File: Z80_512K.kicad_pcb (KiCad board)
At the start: 2 copper layers, 73 x 55.5 mm, 24 parts, among them J1 USB_B_Mini, J2 EXPANSION-BUS, SW1 ON|OFF, SW2 Z80-RESET, U1 Z84C00/PLCC, U2 74HCT574, U3 SRAM-SOP32, U4 74HC138, U5 SST39SF040, U6 74HC74, U7 74HC00, Y1 CXO_DIP14

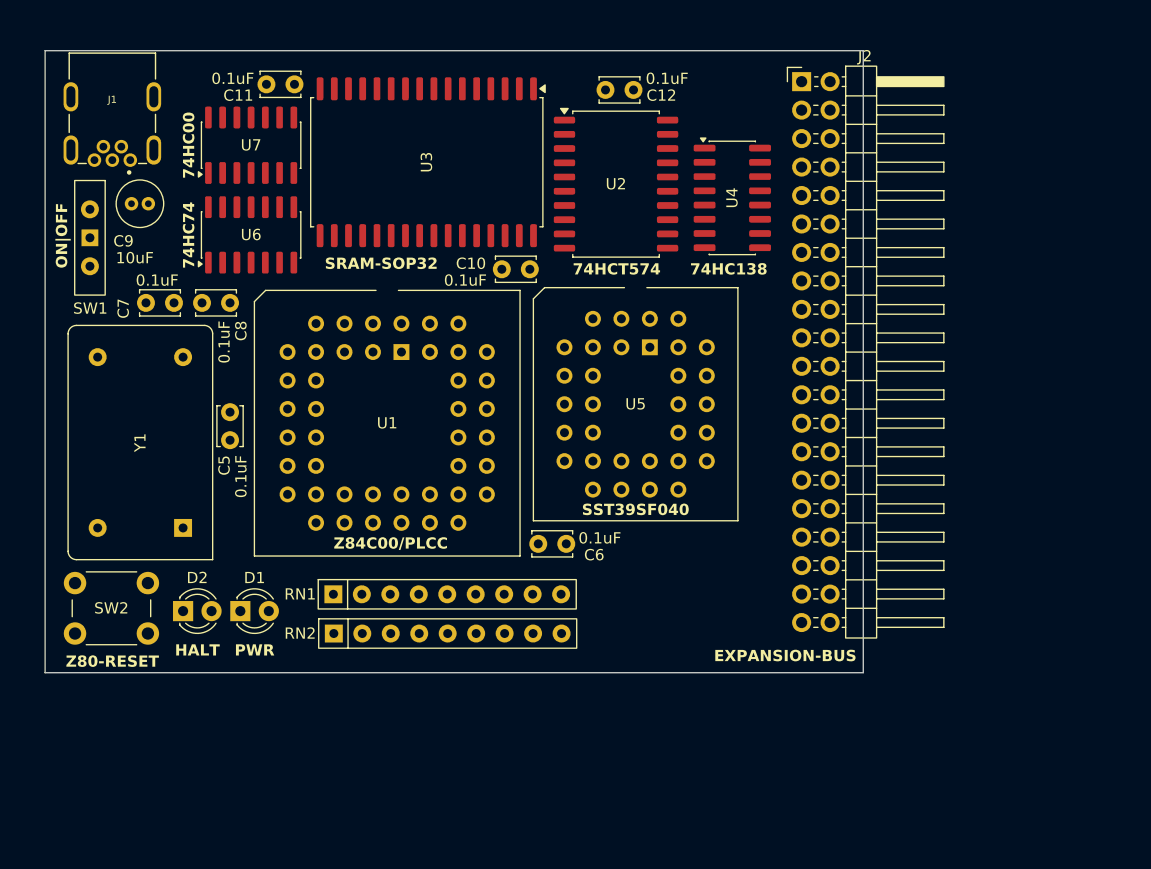
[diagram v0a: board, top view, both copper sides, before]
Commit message: Finished Routing Layout.
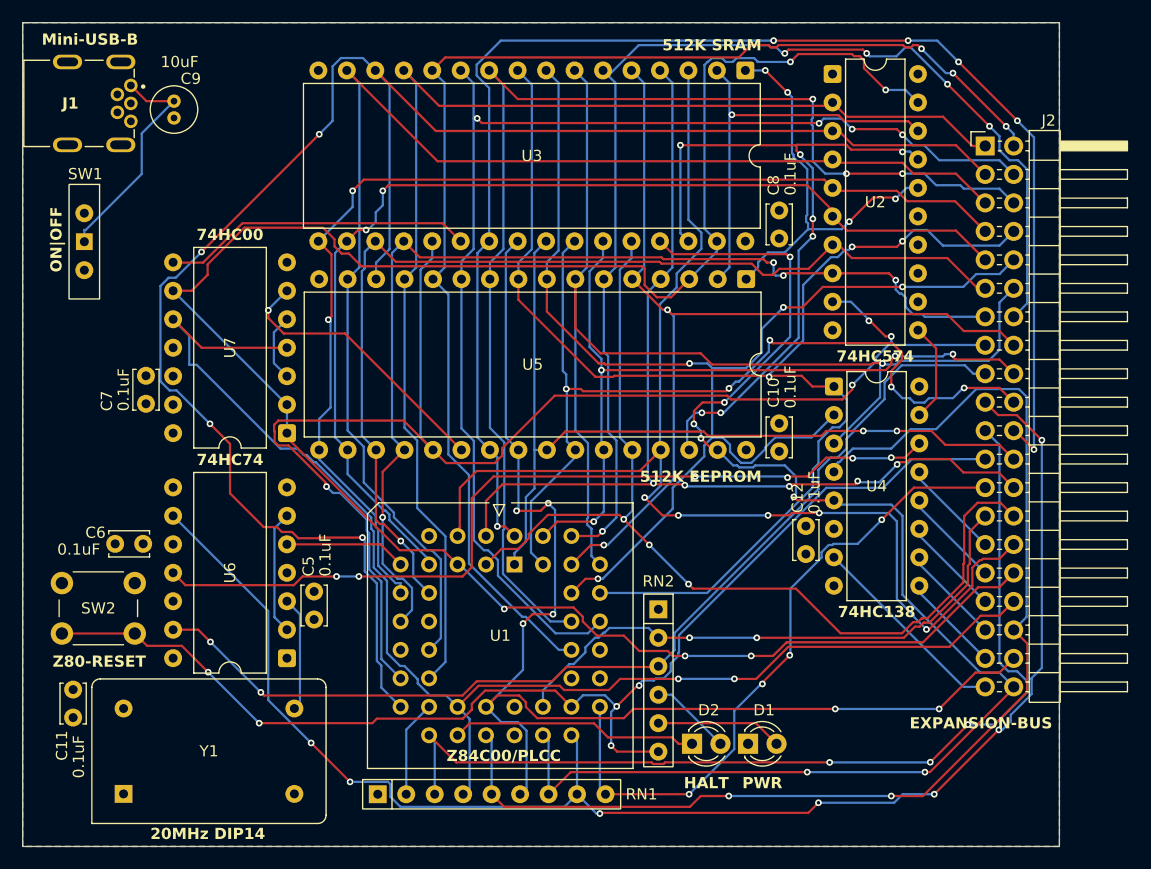
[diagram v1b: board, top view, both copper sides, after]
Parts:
- J1: value USB_B_Mini -> Mini-USB-B
- RN1: value RN_10K -> RN10K
- RN2: value RN_10K -> RN10K; footprint Resistor_THT:R_Array_SIP9 -> Resistor_THT:R_Array_SIP6
- U2: value 74HCT574 -> 74HC574; footprint Package_SO:SOP-20_7.5x12.8mm_P1.27mm -> Package_DIP:DIP-20_W7.62mm
- U3: value SRAM-SOP32 -> 512K SRAM; footprint Package_SO:SOP-32_11.305x20.495mm_P1.27mm -> Package_DIP:DIP-32_W15.24mm
- U4: footprint Package_SO:SOIC-16_3.9x9.9mm_P1.27mm -> Package_DIP:DIP-16_W7.62mm
- U5: value SST39SF040 -> 512K EEPROM; footprint Package_LCC:PLCC-32_THT-Socket -> Package_DIP:DIP-32_W15.24mm
- U6, U7: footprint Package_SO:SOIC-14_3.9x8.7mm_P1.27mm -> Package_DIP:DIP-14_W10.16mm
- Y1: value CXO_DIP14 -> 20MHz DIP14
- moved C11 59.9 mm to (107.0, 93.0), turned to 90 degrees
- moved C8 49.7 mm to (170.0, 47.8), turned to -90 degrees
- moved D2 46.9 mm to (162.2, 95.3)
- moved D1 46.8 mm to (167.2, 95.3)
- moved C12 44.2 mm to (172.4, 78.4), turned to 90 degrees
- moved C6 40.2 mm to (110.8, 77.5), turned to 0 degrees
- moved U6 37.9 mm to (126.1, 87.7), turned to 180 degrees
- moved U3 29.6 mm to (167.0, 35.3)
- moved RN2 29.0 mm to (159.2, 83.3), turned to -90 degrees
- moved C10 26.2 mm to (170.0, 66.8), turned to -90 degrees
- moved U7 25.9 mm to (126.1, 67.6), turned to 180 degrees
- moved Y1 24.3 mm to (111.5, 99.8), turned to 0 degrees
- moved U2 21.7 mm to (174.8, 35.6)
- moved U1 21.5 mm to (146.4, 79.3)
- moved U4 19.1 mm to (174.9, 63.5)
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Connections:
- RN1 pad 2: /MREQ -> /NMI
- RN1 pad 3: /IORQ -> /INT
- RN1 pad 4: /RD -> /MREQ
- RN1 pad 5: /WR -> /IORQ
- RN1 pad 6: /WAIT -> /RD
- RN1 pad 7: /NMI -> /WR
- RN1 pad 8: /BUSREQ -> /WAIT
- RN1 pad 9: /INT -> /BUSREQ
- RN2 pad 2: unconnected-(RN2-R1-Pad2) -> /BUSACK
- RN2 pad 3: unconnected-(RN2-R2-Pad3) -> /WAIT_RE
- RN2 pad 4: unconnected-(RN2-R3-Pad4) -> Net-(D2-A)
- RN2 pad 5: unconnected-(RN2-R4-Pad5) -> Net-(D1-A)
- RN2 pad 6: Net-(D2-A) -> /RESET
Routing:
- net /MEM_A15: track 0.00 -> 189.9 mm, vias 0 -> 5
- net /D1: track 0.00 -> 160.3 mm, vias 0 -> 4
- net /WAIT: track 0.00 -> 133.6 mm, vias 0 -> 7
- net /A10: track 0.00 -> 129.3 mm, vias 0 -> 6
- net /WR: track 0.00 -> 127.1 mm, vias 0 -> 7
- net /D7: track 0.00 -> 125.7 mm, vias 0 -> 4
- net /MREQ: track 0.00 -> 121.2 mm, vias 0 -> 2
- net /D2: track 0.00 -> 118.7 mm
- net /A3: track 0.00 -> 118.4 mm, vias 0 -> 3
- net /A0: track 0.00 -> 116.0 mm, vias 0 -> 3
- net /D0: track 0.00 -> 112.2 mm
- net /A4: track 0.00 -> 111.6 mm, vias 0 -> 4
- net /RD: track 0.00 -> 111.4 mm, vias 0 -> 6
- net /A14: track 0.00 -> 110.8 mm, vias 0 -> 5
- net /A1: track 0.00 -> 109.8 mm, vias 0 -> 4
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- added copper zone on B.Cu, net GND
- added copper zone on F.Cu, net VCC
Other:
- board size 73 x 55.5 mm -> 92.5 x 73.5 mm
